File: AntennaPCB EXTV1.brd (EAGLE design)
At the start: 43.2 x 43.2 mm, 28 parts, among them J1 BM02B-ACHSS-GAN-TF(LF)(SN), Q1 27.12MHz

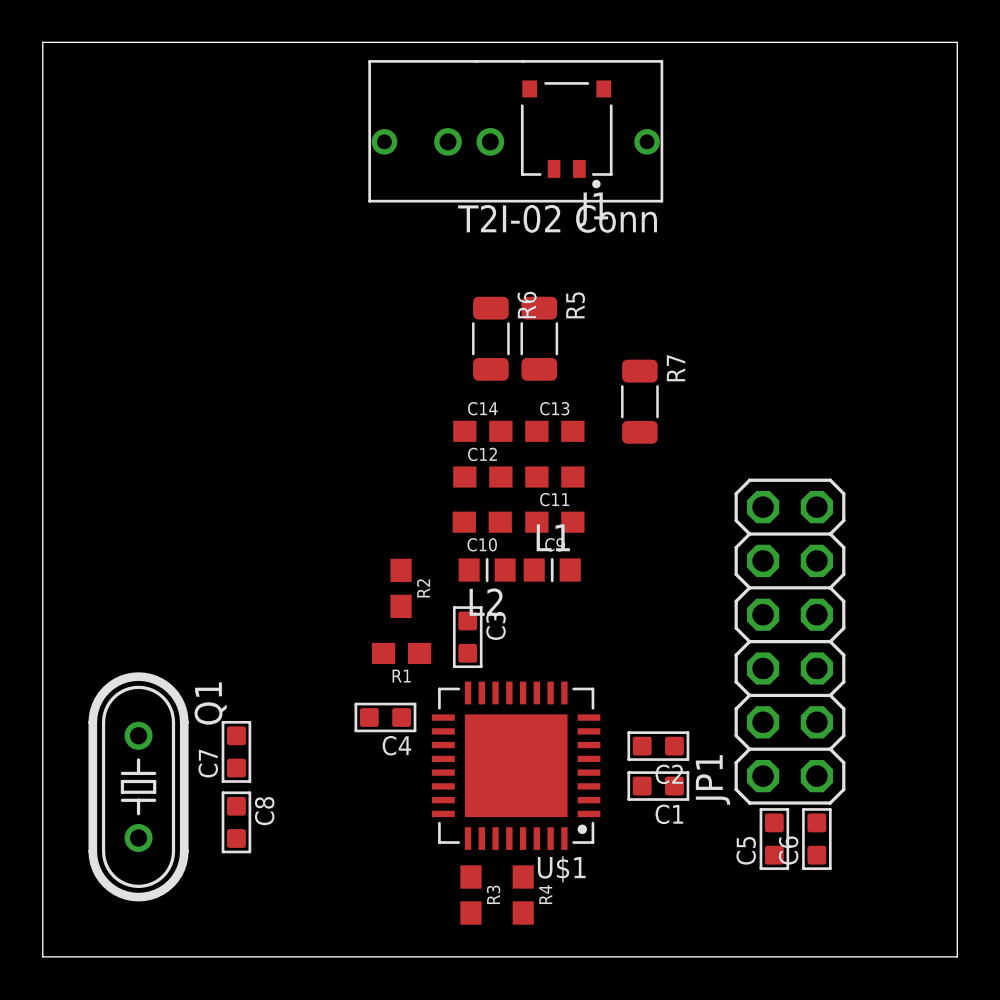
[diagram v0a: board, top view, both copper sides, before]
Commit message: Repositioning components on board
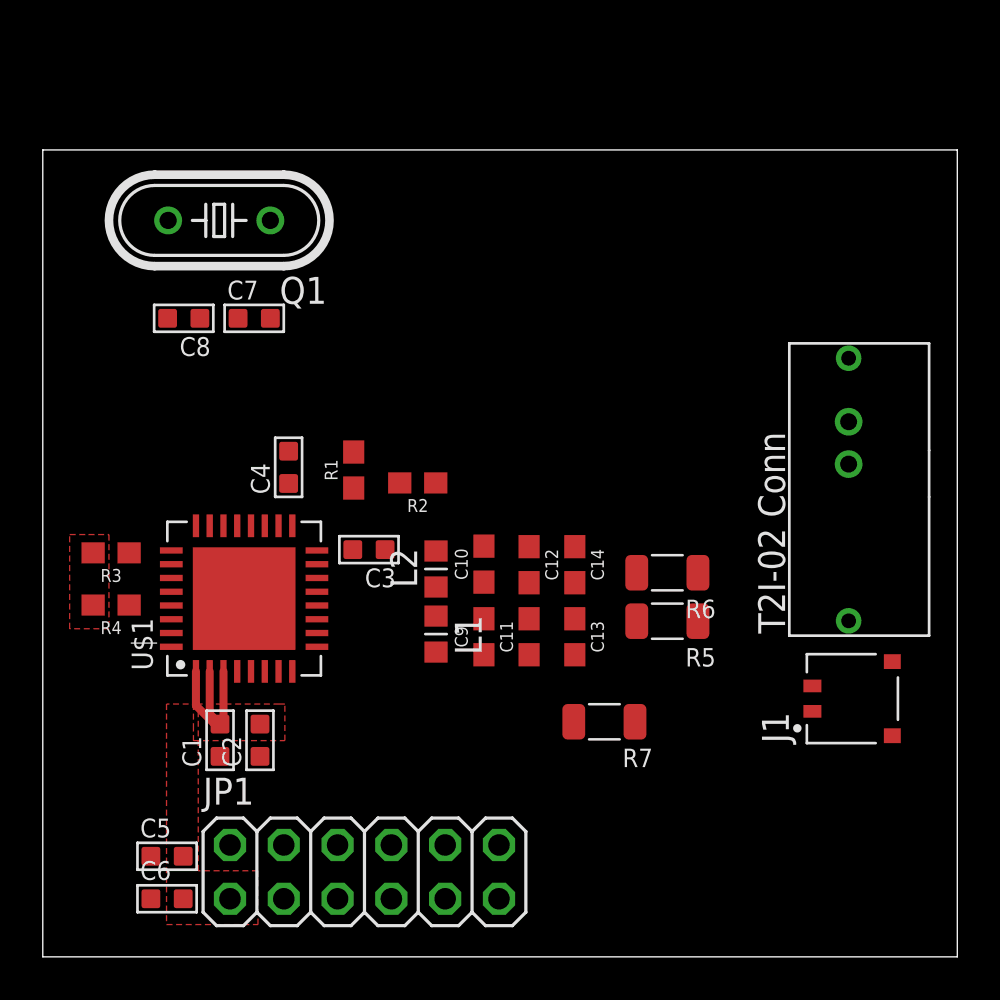
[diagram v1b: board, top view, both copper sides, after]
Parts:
- J1: value BM02B-ACHSS-GAN-TF(LF)(SN) -> (none)
- moved C6 30.8 mm to (5.87, 2.74), turned to 90 degrees
- moved J1 30.1 mm to (38.2, 12.2), turned to 90 degrees
- moved C5 28.7 mm to (5.87, 4.75), turned to 90 degrees
- moved Q1 27.0 mm to (8.33, 34.8), turned to 180 degrees
- moved C8 23.9 mm to (6.65, 30.1), turned to 270 degrees
- moved R4 23.8 mm to (3.23, 16.6), turned to 180 degrees
- moved R3 23.4 mm to (3.23, 19.1), turned to 180 degrees
- moved JP1 22.8 mm to (15.2, 4.01), turned to 0 degrees
- moved U$2 22.8 mm to (38.0, 23.3), turned to 90 degrees
- moved C1 20.8 mm to (8.37, 10.2), turned to 180 degrees
- moved C7 20.5 mm to (9.98, 30.1), turned to 90 degrees
- moved C2 18.8 mm to (10.3, 10.2), turned to 180 degrees
- moved R7 15.2 mm to (26.5, 11.1), turned to 180 degrees
- moved R5 14.6 mm to (29.5, 15.8), turned to 180 degrees
- moved R6 13.8 mm to (29.5, 18.1), turned to 180 degrees
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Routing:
- net 3.3V: track 0.00 -> 8.36 mm
- added copper zone on layer 1, net 3.3V
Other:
- board size 43.2 x 43.2 mm -> 43.2 x 38.1 mm

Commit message: Re-created some parts on a schematic and did some more positioning adjustments as well as DRC
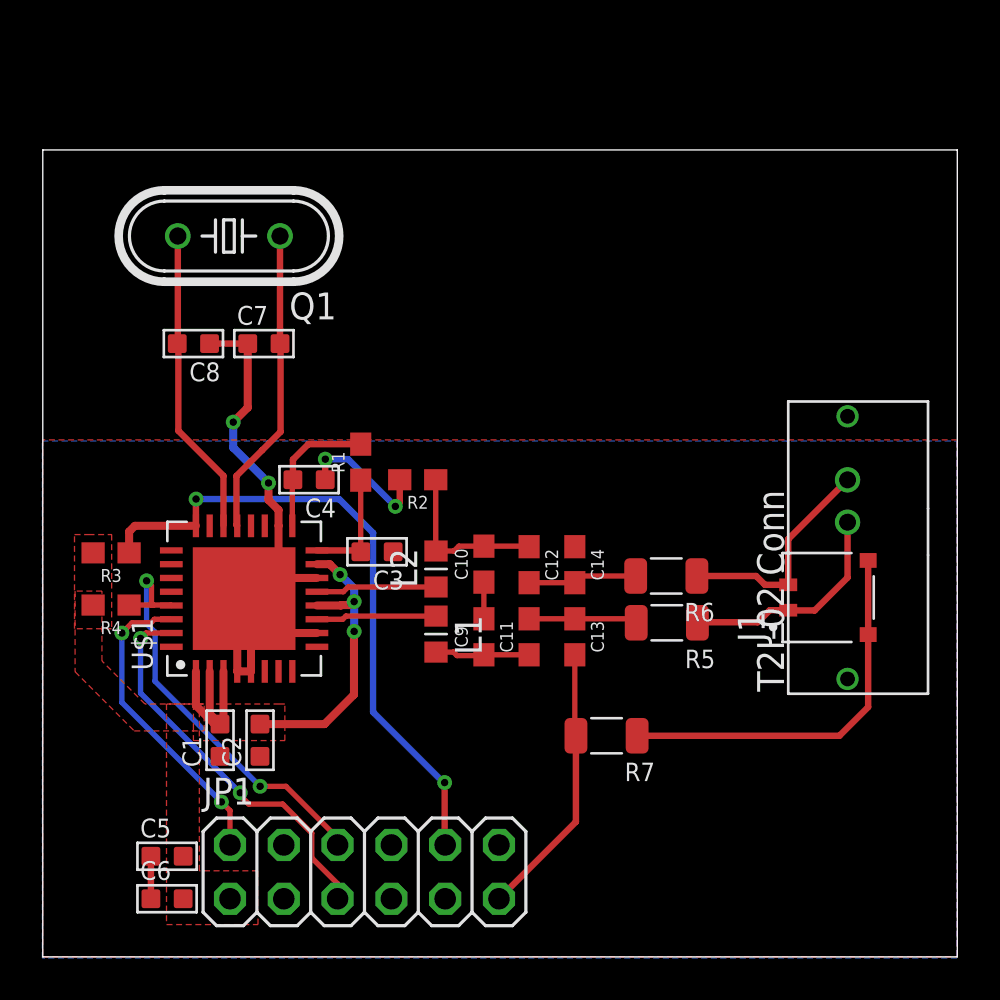
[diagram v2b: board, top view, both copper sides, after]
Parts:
- C7, C8: value 1uf -> 7pF
- moved J1 4.91 mm to (37.1, 17.0)
- moved U$2 2.74 mm to (38.0, 20.5)
- moved C8 1.28 mm to (7.11, 29.0)
- moved C7 1.28 mm to (10.4, 29.0)
- moved C4 1.13 mm to (12.6, 22.5), turned to 270 degrees
- moved Q1 0.87 mm to (8.79, 34.0)
- moved R7 0.67 mm to (26.6, 10.4)
- moved R1 0.50 mm to (15.0, 23.4)
- moved C3 0.39 mm to (15.8, 19.1)
- moved R6 0.16 mm to (29.4, 18.0)
- moved R2 0.15 mm to (17.7, 22.5)
- moved R5 0.08 mm to (29.5, 15.8)
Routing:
- net GND: track 0.00 -> 46.4 mm, vias 0 -> 2
- net SS: track 0.00 -> 30.8 mm, vias 0 -> 2
- net SCLK: track 0.00 -> 20.2 mm, vias 0 -> 2
- net MISO: track 0.00 -> 18.6 mm, vias 0 -> 2
- net N$7: track 0.00 -> 18.4 mm
- net MOSI: track 0.00 -> 14.7 mm, vias 0 -> 2
- net N$5: track 0.00 -> 14.6 mm
- net N$6: track 0.00 -> 14.6 mm
- net 3.3V: track 8.36 -> 22.4 mm, vias 0 -> 3
- net ANTC_2: track 0.00 -> 10.6 mm
- net ANTC_1: track 0.00 -> 10.6 mm
- net RC: track 0.00 -> 7.87 mm
- net N$2: track 0.00 -> 6.66 mm
- net N$3: track 0.00 -> 6.55 mm, vias 0 -> 2
- net ANT_2: track 0.00 -> 5.72 mm
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- added copper zone on layer 1, net GND
- added copper zone on layer 16, net GND

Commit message: Created the antenna board and adjusted sizing of the board
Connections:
- removed net RST: U$1.6
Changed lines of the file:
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@@
 <wire x1="18.9738" y1="5.3086" x2="18.9992" y2="5.2832" width="0.3048" layer="1"/>
-</signal>
-<signal name="RST">
-<contactref element="U$1" pad="6"/>
 </signal>
 <signal name="ANT_1">

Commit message: Moved more stuff around and edited via sizes
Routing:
- net GND: vias 2 -> 8

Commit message: Put stand-offs on the board
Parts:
- added H1, H2, H3: STAND-OFF, SparkFun-Hardware:STAND-OFF
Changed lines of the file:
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@@
 <element name="U$1" library="SeniorDesignParts" package="HVQFN32" value="MFRC522" x="12.6812" y="13.7404" rot="R90"/>
 <element name="U$2" library="SeniorDesignParts" package="T2I-02" value="T2I-02" x="37.9984" y="20.5232" rot="R90"/>
+<element name="H1" library="SparkFun-Hardware" library_urn="urn:adsk.eagle:library:519" package="STAND-OFF" package3d_urn="urn:adsk.eagle:package:38630/1" value="STAND-OFF" x="40" y="3.2"/>
+<element name="H2" library="SparkFun-Hardware" library_urn="urn:adsk.eagle:library:519" package="STAND-OFF" package3d_urn="urn:adsk.eagle:package:38630/1" value="STAND-OFF" x="40" y="34"/>
+<element name="H3" library="SparkFun-Hardware" library_urn="urn:adsk.eagle:library:519" package="STAND-OFF" package3d_urn="urn:adsk.eagle:package:38630/1" value="STAND-OFF" x="2.9" y="27"/>
 </elements>
 <signals>

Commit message: moved Standoffs
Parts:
- moved H1 5.00 mm to (35.0, 3.20)
- moved H2 5.00 mm to (35.0, 34.0)
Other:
- board text added: "EXT Antenna Board V1 ECE477 GRP15 Melchor De La Garza Cynthia Zatlokowicz"
